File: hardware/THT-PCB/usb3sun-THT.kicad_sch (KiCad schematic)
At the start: 44 parts, among them J2 8918-P8B, J3 USB-U267-BWS, Q1 2N7002DW, Q3 2N7002DW, Q7 2N7002DW, SW1 TS-1187A-B-A-B, U1 Pico, U2 SRV05-4, U3 SRV05-4, U4 MAX40200AUK, U5 MAX40200AUK

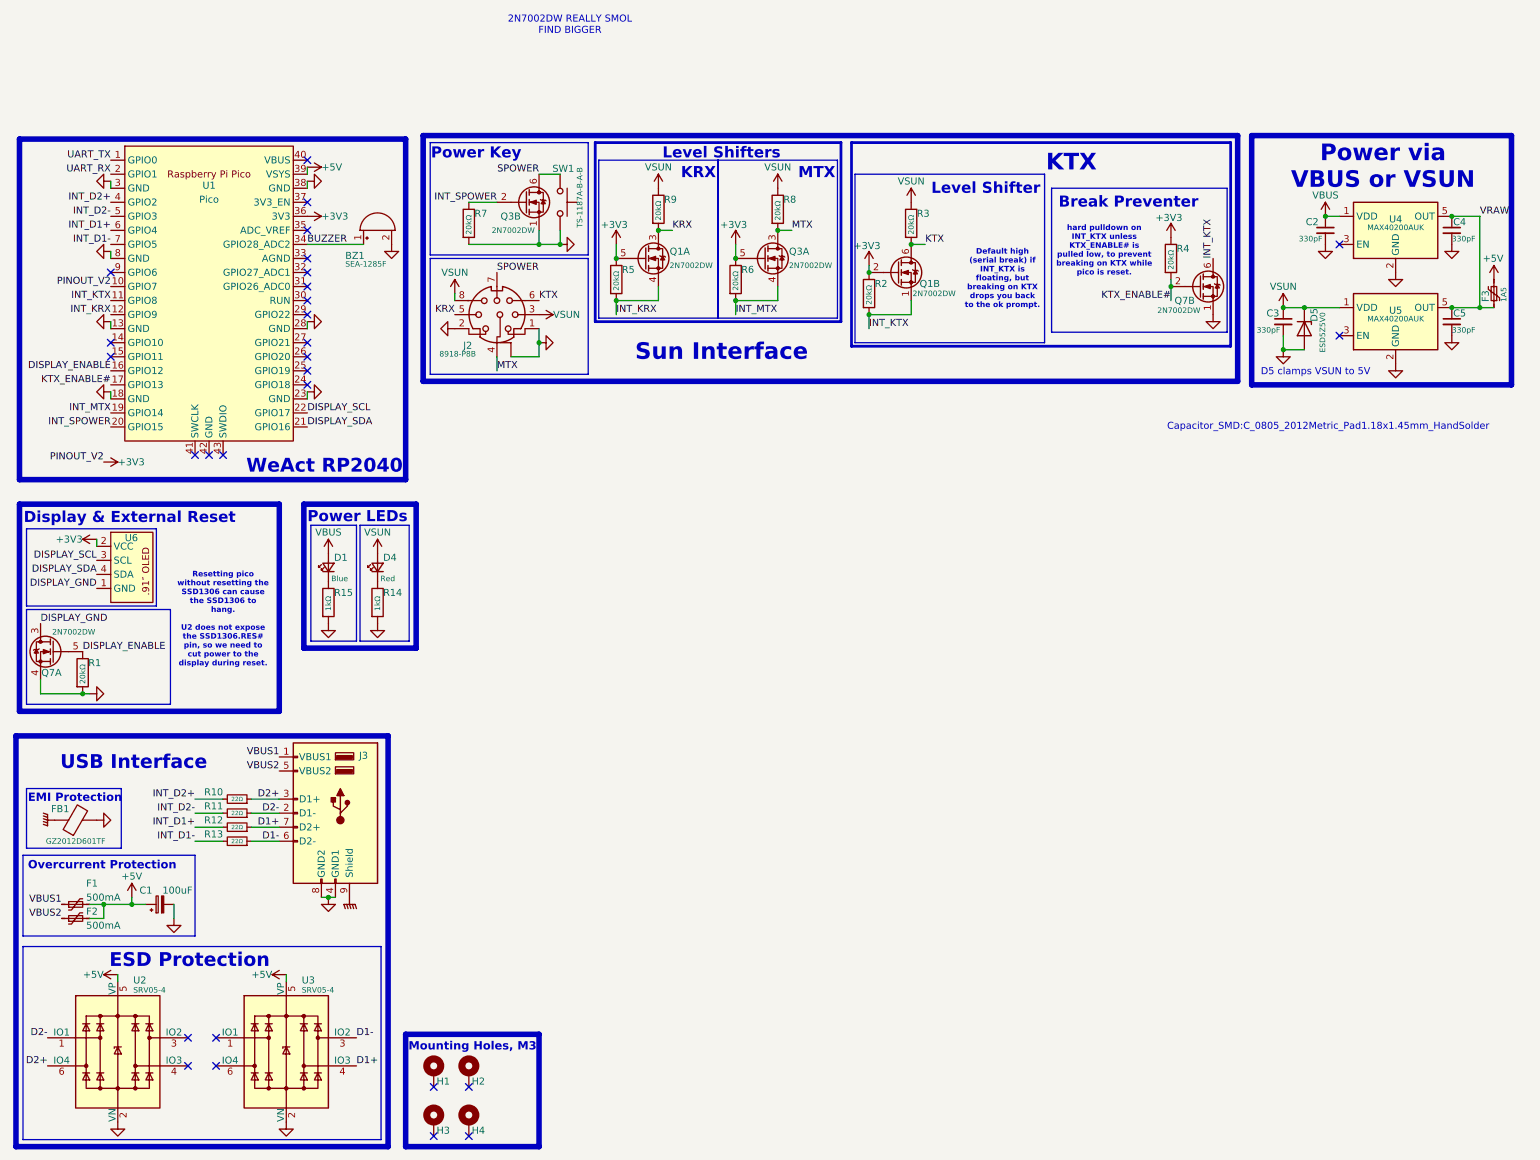
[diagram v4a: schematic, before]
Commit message: Complete PCB layout, Further schematic adjustments; TODO traces
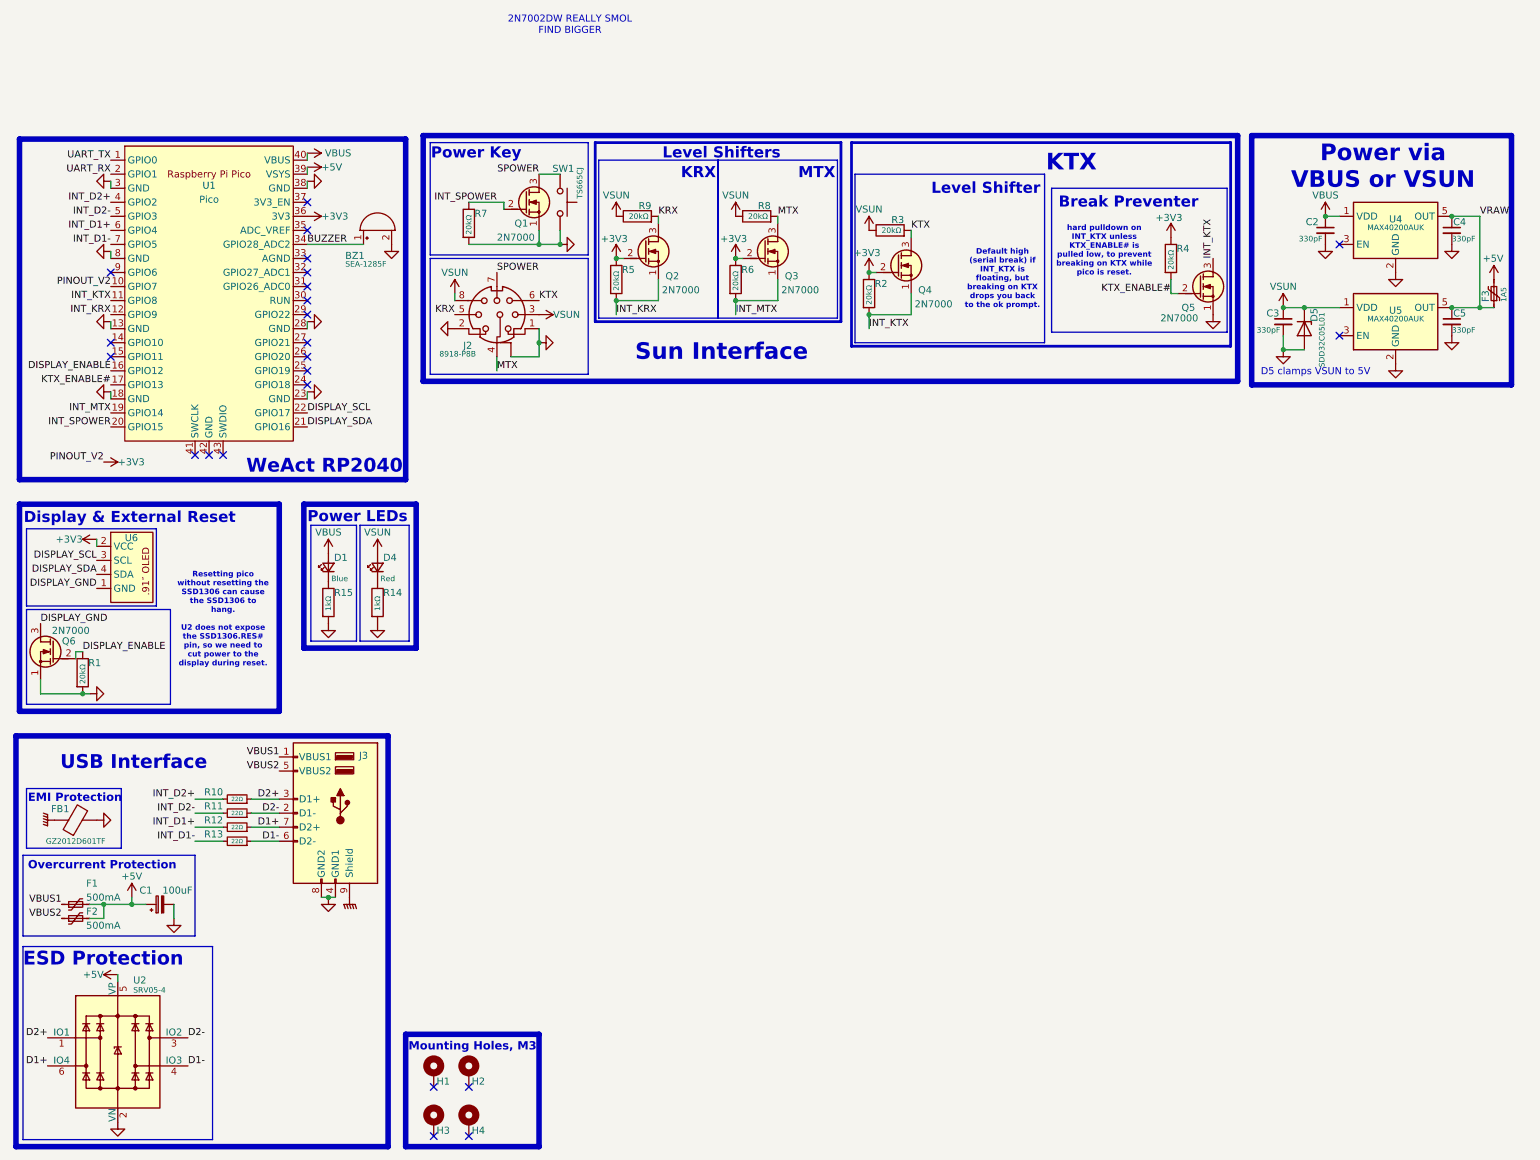
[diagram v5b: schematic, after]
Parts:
- removed Q1, Q3, Q7: 2N7002DW, Package_TO_SOT_SMD:SOT-363_SC-70-6, symbol usb3sun:2N7002DW
- removed U3: SRV05-4, marbastlib-various:SOT-23-6-routable, symbol marbastlib-various:SRV05-4
- added Q1, Q2, Q3, Q4, Q5, Q6: 2N7000, Package_TO_SOT_THT:TO-92_Inline, symbol PCM_Transistor_MOSFET_AKL:2N7000
- C2, C3, C4, C5: footprint Capacitor_SMD:C_0805_2012Metric_Pad1.18x1.45mm_HandSolder -> Capacitor_THT:C_Disc_D3.8mm_W2.6mm_P2.50mm; LCSC C376975 -> C94711
- D5: value ESD5Z5V0 -> SDD32C05L01; footprint Diode_SMD:D_SOD-523 -> Diode_SMD:D_SOD-323_HandSoldering; LCSC C502546 -> C313311
- R10, R11, R12, R13: LCSC C25092 -> (none)
- SW1: value TS-1187A-B-A-B -> TS665CJ; footprint Button_Switch_SMD:SW_Push_1P1T_XKB_TS-1187A -> Button_Switch_THT:SW_PUSH_6mm_H4.3mm; LCSC C318884 -> C5340136
- U4, U5: footprint Package_TO_SOT_SMD:SOT-23-5 -> Package_TO_SOT_SMD:SOT-23-5_HandSoldering
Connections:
- net +3V3: now also Q2.2 (G), Q3.2 (G), Q4.2 (G)
- net D1+: now also U2.6 (IO4)
- net D1-: now also U2.4 (IO3)
- net D2+: now also U2.1 (IO1); no longer U2.6 (IO4)
- net D2-: now also U2.3 (IO2); no longer U2.1 (IO1)
- net DISPLAY_ENABLE: now also Q6.2 (G)
- net DISPLAY_GND: now also Q6.3 (D)
- net GND: now also Q1.1 (S), Q5.1 (S), Q6.1 (S)
- net INT_KRX: now also Q2.1 (S)
- net INT_KTX: now also Q4.1 (S), Q5.3 (D)
- net INT_MTX: now also Q3.1 (S)
- net INT_SPOWER: now also Q1.2 (G)
- net KRX: now also Q2.3 (D)
- net KTX: now also Q4.3 (D)
- net KTX_ENABLE#: now also Q5.2 (G)
- net MTX: now also Q3.3 (D)
- net SPOWER: now also Q1.3 (D)
- net VBUS: now also U1.40 (VBUS)
- no-connect marks 28 -> 23
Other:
- note removed: "Capacitor_SMD:C_0805_2012Metric_Pad1.18x1.45mm_HandSolder"
- moved on the sheet: R9

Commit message: Fully Routed
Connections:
- net D1+: now also R10.1, U2.1 (IO1); no longer R12.1, U2.6 (IO4)
- net D1-: now also R12.1, U2.6 (IO4); no longer R13.1, U2.4 (IO3)
- net D2+: now also R11.1, U2.3 (IO2); no longer R10.1, U2.1 (IO1)
- net D2-: now also R13.1, U2.4 (IO3); no longer R11.1, U2.3 (IO2)
- net INT_D1+: now also R10.2; no longer R12.2
- net INT_D1-: now also R12.2; no longer R13.2
- net INT_D2+: now also R11.2; no longer R10.2
- net INT_D2-: now also R13.2; no longer R11.2
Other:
- note removed: "2N7002DW REALLY SMOL FIND BIGGER"

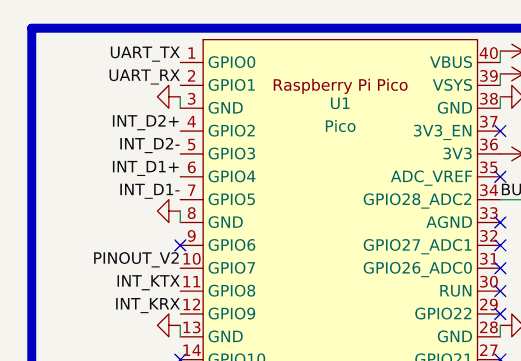
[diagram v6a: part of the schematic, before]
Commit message: Add UART Header
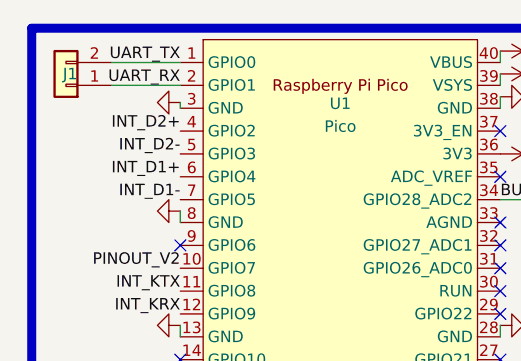
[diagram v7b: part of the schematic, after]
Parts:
- added J1: Conn_01x02, Connector_PinHeader_2.54mm:PinHeader_1x02_P2.54mm_Vertical, symbol Connector_Generic:Conn_01x02
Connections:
- net UART_RX: now also J1.1 (Pin_1)
- net UART_TX: now also J1.2 (Pin_2)
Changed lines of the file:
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@@
 	(wire
 		(pts
+			(xy 22.86 20.32) (xy 30.48 20.32)
+		)
+		(stroke
+			(width 0)
+			(type default)
+		)
+	)
+	(wire
+		(pts
 			(xy 107.95 33.02) (xy 111.76 33.02)
 		)
@@
 	(wire
 		(pts
+			(xy 22.86 17.78) (xy 30.48 17.78)
+		)
+		(stroke
+			(width 0)
+			(type default)
+		)
+	)
+	(wire
+		(pts
 			(xy 111.76 30.48) (xy 111.76 33.02)
 		)
@@
 	(wire
 		(pts
-			(xy 30.48 21.59) (xy 30.48 22.86)
+			(xy 30.48 22.225) (xy 30.48 22.86)
 		)
 		(stroke
@@
 	)
 	(symbol
+		(lib_id "Connector_Generic:Conn_01x02")
+		(at 17.78 20.32 180)
+		(unit 1)
+		(exclude_from_sim no)
+		(in_bom yes)
+		(on_board yes)
+		(dnp no)
+		(property "Reference" "J1"
+			(at 19.05 19.05 0)
+			(effects
+				(font
+					(size 1.27 1.27)
+				)
+				(justify left)
+			)
+		)
+		(property "Value" "Conn_01x02"
+			(at 14.605 17.7801 0)
+			(effects
+				(font
+					(size 1.27 1.27)
+				)
+				(justify left)
+				(hide yes)
+			)
+		)
+		(property "Footprint" "Connector_PinHeader_2.54mm:PinHeader_1x02_P2.54mm_Vertical"
+			(at 17.78 20.32 0)
+			(effects
+				(font
+					(size 1.27 1.27)
+				)
+				(hide yes)
+			)
+		)
+		(property "Datasheet" "~"
+			(at 17.78 20.32 0)
+			(effects
+				(font
+					(size 1.27 1.27)
+				)
+				(hide yes)
+			)
+		)
+		(property "Description" "Generic connector, single row, 01x02, script generated (kicad-library-utils/schlib/autogen/connector/)"
+			(at 17.78 20.32 0)
+			(effects
+				(font
+					(size 1.27 1.27)
+				)
+				(hide yes)
+			)
+		)
+		(pin "2"
+		)
+		(pin "1"
+		)
+		(instances
+			(project "usb3sun-THT"
+				(path "/e8fc4e41-10af-441f-8282-dd879bdc5d08"
+					(reference "J1")
+					(unit 1)
+				)
+			)
+		)
+	)
+	(symbol
 		(lib_id "power:GND")
 		(at 111.76 33.02 90)
@@
 	(symbol
 		(lib_id "power:GND")
-		(at 30.48 21.59 270)
+		(at 30.48 22.225 270)
 		(unit 1)
 		(exclude_from_sim no)
@@
 		(fields_autoplaced yes)
 		(property "Reference" "#PWR05"
-			(at 24.13 21.59 0)
+			(at 24.13 22.225 0)
 			(effects
 				(font
@@
 		)
 		(property "Value" "GND"
-			(at 25.4 21.59 0)
+			(at 25.4 22.225 0)
 			(effects
 				(font
@@
 		)
 		(property "Footprint" ""
-			(at 30.48 21.59 0)
+			(at 30.48 22.225 0)
 			(effects
 				(font
@@
 		)
 		(property "Datasheet" ""
-			(at 30.48 21.59 0)
+			(at 30.48 22.225 0)
 			(effects
 				(font
@@
 		)
 		(property "Description" "Power symbol creates a global label with name \"GND\" , ground"
-			(at 30.48 21.59 0)
+			(at 30.48 22.225 0)
 			(effects
 				(font

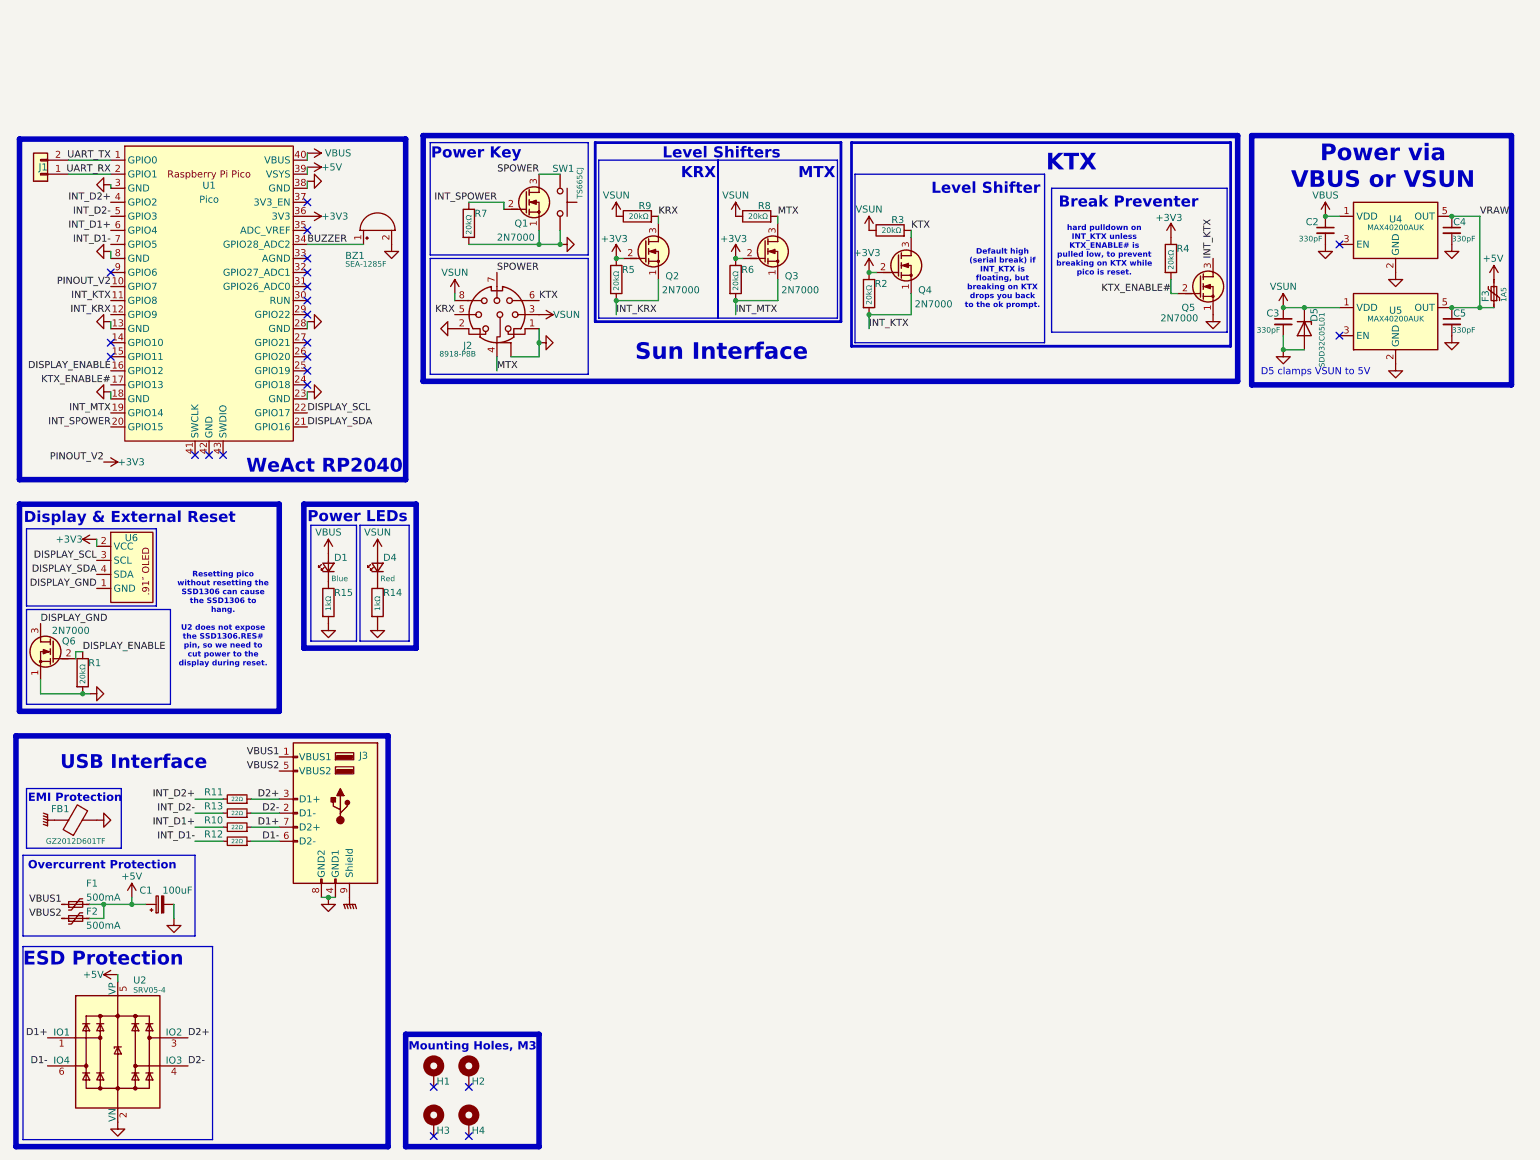
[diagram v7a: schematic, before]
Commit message: Fix Sun connector, add connector config jumpers
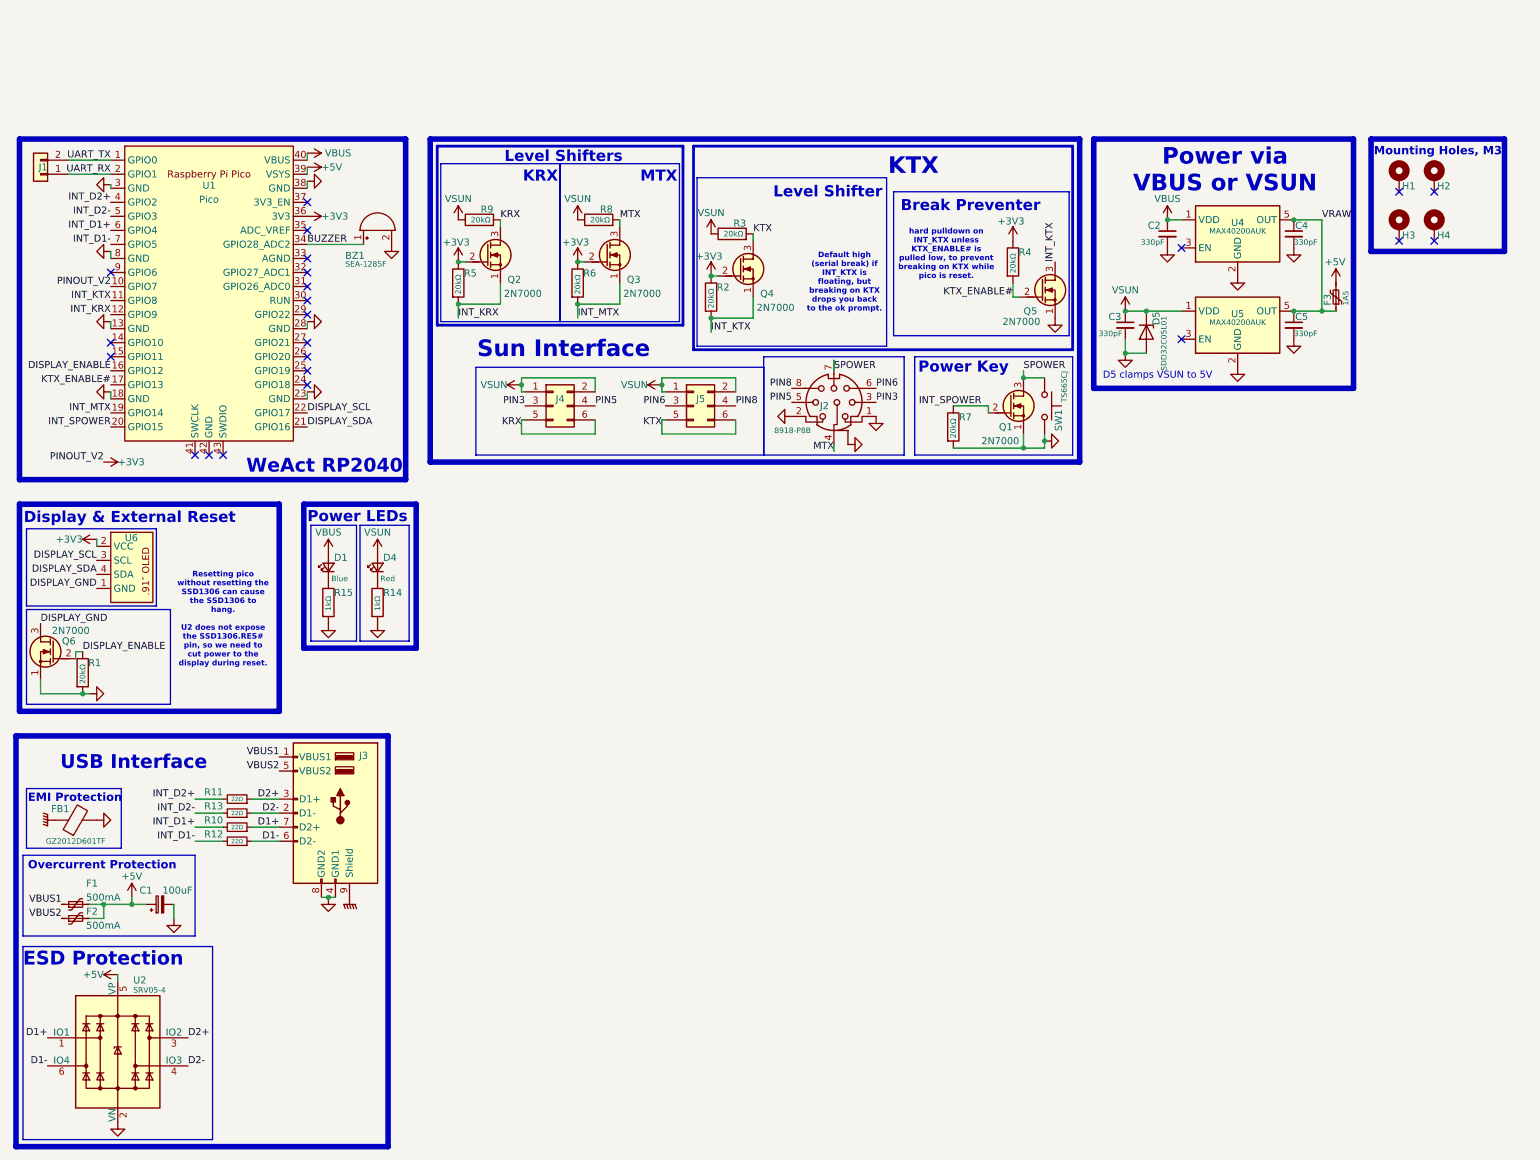
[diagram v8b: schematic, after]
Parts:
- added J4, J5: Conn_02x03_Odd_Even, Connector_PinHeader_2.54mm:PinHeader_2x03_P2.54mm_Vertical, symbol Connector_Generic:Conn_02x03_Odd_Even
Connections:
- net KRX: now also J4.5 (Pin_5), J4.6 (Pin_6); no longer J2.5
- net KTX: now also J5.5 (Pin_5), J5.6 (Pin_6); no longer J2.6
- net VSUN: now also J4.1 (Pin_1), J4.2 (Pin_2), J5.1 (Pin_1), J5.2 (Pin_2); no longer J2.3, J2.8
- new net PIN3: J2.3, J4.3 (Pin_3)
- new net PIN5: J2.5, J4.4 (Pin_4)
- new net PIN6: J2.6, J5.3 (Pin_3)
- new net PIN8: J2.8, J5.4 (Pin_4)
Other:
- moved on the sheet: C2, C3, C4, C5, D5, F3, H1, H2, H3, H4, J2, Q1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
